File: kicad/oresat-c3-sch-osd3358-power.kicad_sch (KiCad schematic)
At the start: 37 parts, among them Q6 MMBT2907, U1 OSD3358-512M-BSM, U10 SN74LVC1G07DCK, U14 TLVH431

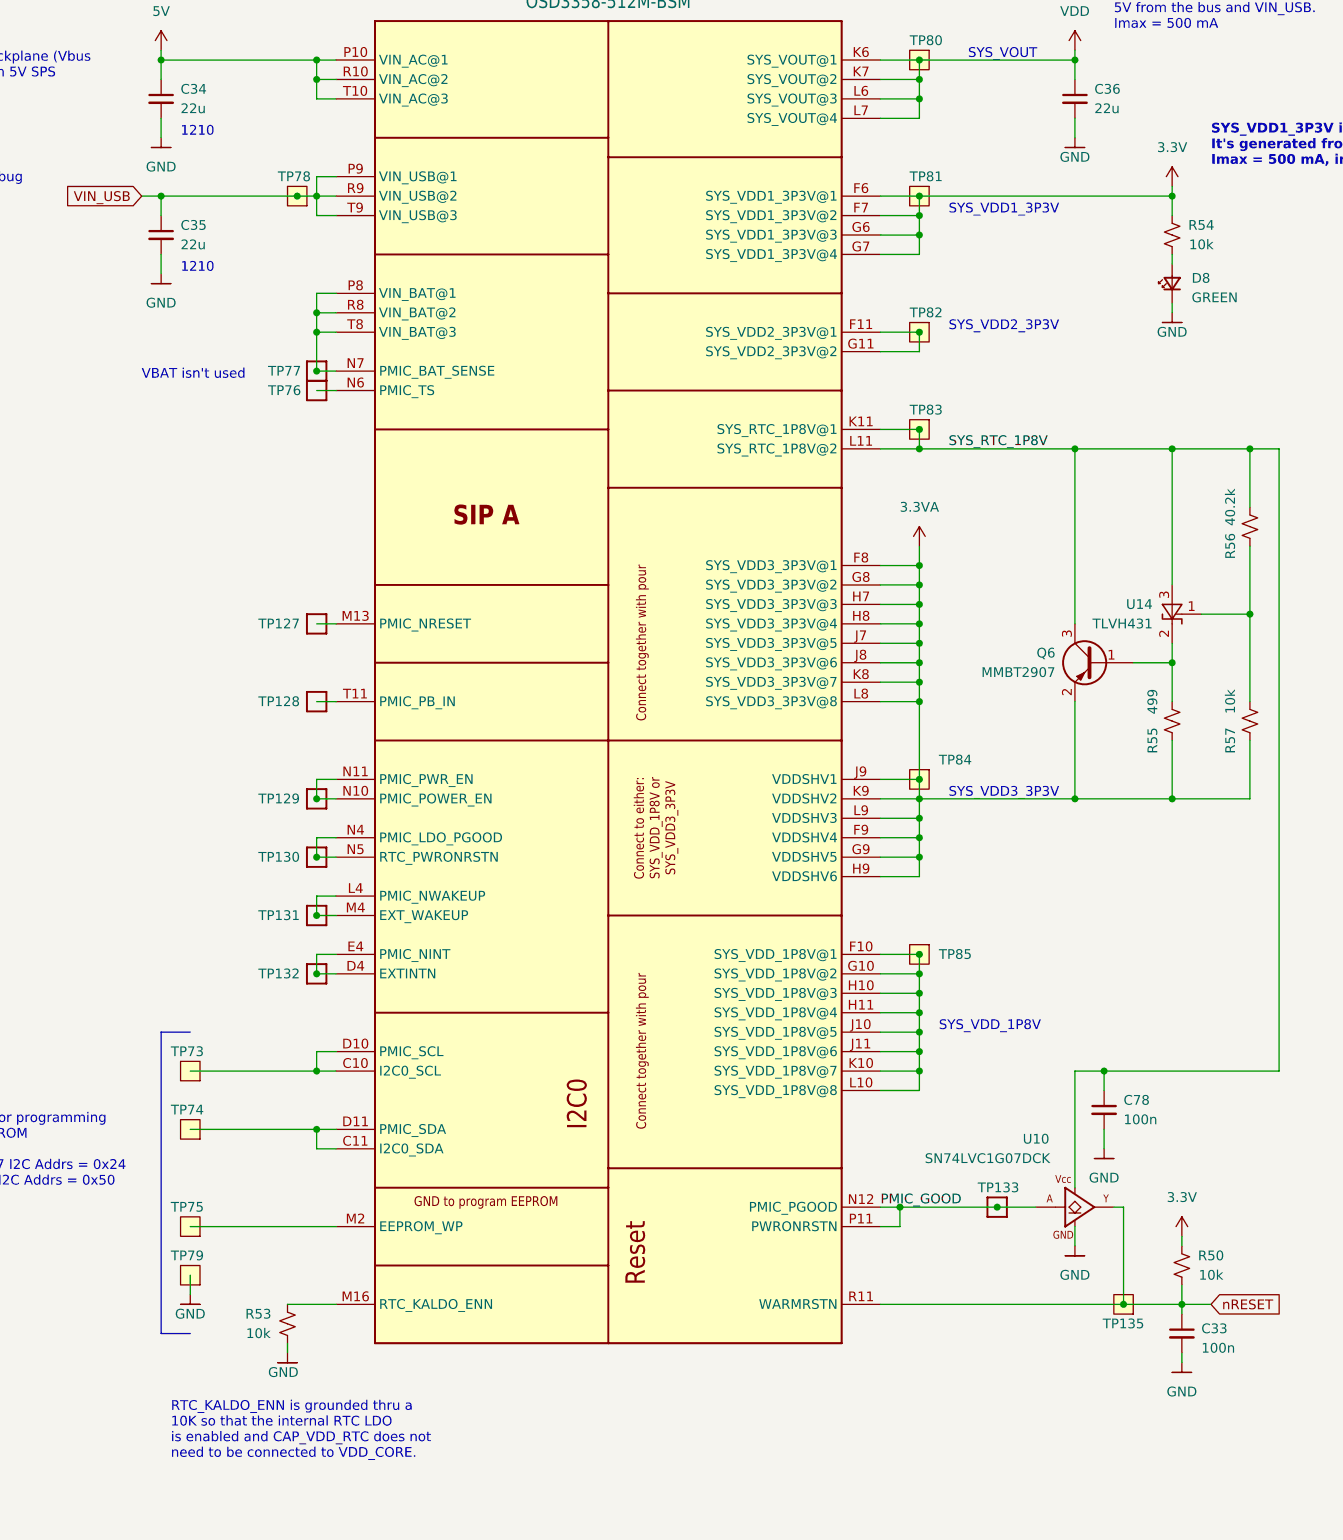
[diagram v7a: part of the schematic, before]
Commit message: Fixed footprints and laid out WDT and OPD circuitry.
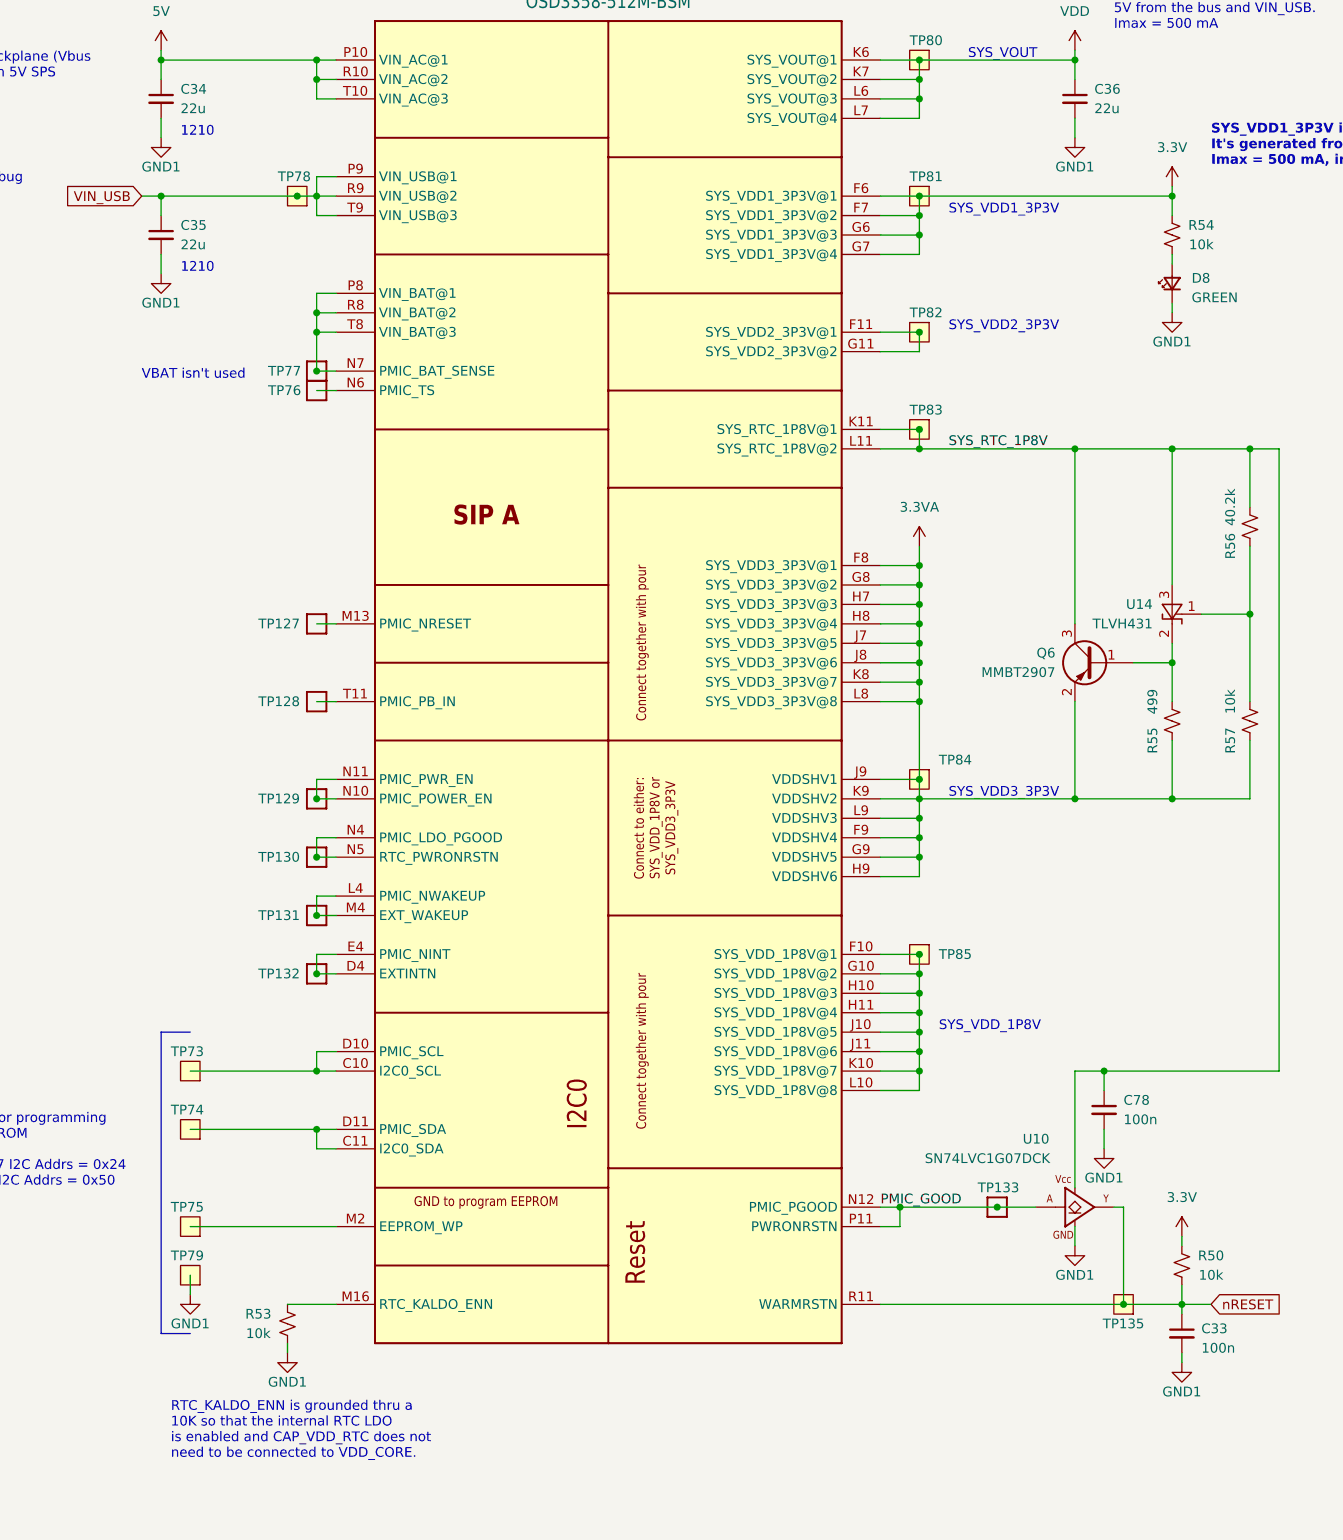
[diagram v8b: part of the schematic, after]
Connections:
- net GND renamed GND1
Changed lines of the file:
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@@
     )
   )
-  (symbol (lib_id "oresat-power:GND") (at 298.45 86.36 0) (unit 1)
-    (in_bom yes) (on_board yes) (dnp no)
-    (property "Reference" "#GND0175" (at 298.45 92.71 0)
-      (effects (font (size 1.27 1.27)) hide)
-    )
-    (property "Value" "GND" (at 298.45 88.9 0)
+  (symbol (lib_id "power:GND1") (at 298.45 86.36 0) (unit 1)
+    (in_bom yes) (on_board yes) (dnp no)
+    (property "Reference" "#PWR0140" (at 298.45 92.71 0)
+      (effects (font (size 1.27 1.27)) hide)
+    )
+    (property "Value" "GND1" (at 298.45 90.17 0)
       (effects (font (size 1.27 1.27)))
     )
@@
       (project "oresat-c3"
         (path "/65d12cdd-c326-4033-9053-c59fa4e0b25e/0c1da208-2d1c-4d05-9cc7-59584e50a6ac"
-          (reference "#GND0175") (unit 1)
+          (reference "#PWR0140") (unit 1)
         )
       )
@@
     )
   )
-  (symbol (lib_id "oresat-power:GND") (at 289.56 195.58 0) (unit 1)
-    (in_bom yes) (on_board yes) (dnp no) (fields_autoplaced)
-    (property "Reference" "#GND0170" (at 289.56 201.93 0)
-      (effects (font (size 1.27 1.27)) hide)
-    )
-    (property "Value" "GND" (at 289.56 199.39 0)
+  (symbol (lib_id "power:GND1") (at 289.56 195.58 0) (unit 1)
+    (in_bom yes) (on_board yes) (dnp no) (fields_autoplaced)
+    (property "Reference" "#PWR0137" (at 289.56 201.93 0)
+      (effects (font (size 1.27 1.27)) hide)
+    )
+    (property "Value" "GND1" (at 289.56 199.39 0)
       (effects (font (size 1.27 1.27)))
     )
@@
       (project "oresat-c3"
         (path "/65d12cdd-c326-4033-9053-c59fa4e0b25e/0c1da208-2d1c-4d05-9cc7-59584e50a6ac"
-          (reference "#GND0170") (unit 1)
+          (reference "#PWR0137") (unit 1)
         )
       )
@@
     )
   )
-  (symbol (lib_id "oresat-power:GND") (at 285.75 63.5 0) (unit 1)
-    (in_bom yes) (on_board yes) (dnp no)
-    (property "Reference" "#GND0174" (at 285.75 69.85 0)
-      (effects (font (size 1.27 1.27)) hide)
-    )
-    (property "Value" "GND" (at 285.75 66.04 0)
+  (symbol (lib_id "power:GND1") (at 285.75 63.5 0) (unit 1)
+    (in_bom yes) (on_board yes) (dnp no)
+    (property "Reference" "#PWR0139" (at 285.75 69.85 0)
+      (effects (font (size 1.27 1.27)) hide)
+    )
+    (property "Value" "GND1" (at 285.75 67.31 0)
       (effects (font (size 1.27 1.27)))
     )
@@
       (project "oresat-c3"
         (path "/65d12cdd-c326-4033-9053-c59fa4e0b25e/0c1da208-2d1c-4d05-9cc7-59584e50a6ac"
-          (reference "#GND0174") (unit 1)
-        )
-      )
-    )
-  )
-  (symbol (lib_id "oresat-power:GND") (at 182.88 222.25 0) (unit 1)
-    (in_bom yes) (on_board yes) (dnp no)
-    (property "Reference" "#GND0171" (at 182.88 228.6 0)
-      (effects (font (size 1.27 1.27)) hide)
-    )
-    (property "Value" "GND" (at 180.34 224.79 0)
-      (effects (font (size 1.27 1.27)) (justify left))
+          (reference "#PWR0139") (unit 1)
+        )
+      )
+    )
+  )
+  (symbol (lib_id "power:GND1") (at 182.88 222.25 0) (unit 1)
+    (in_bom yes) (on_board yes) (dnp no)
+    (property "Reference" "#PWR0143" (at 182.88 228.6 0)
+      (effects (font (size 1.27 1.27)) hide)
+    )
+    (property "Value" "GND1" (at 182.88 226.06 0)
+      (effects (font (size 1.27 1.27)))
     )
     (property "Footprint" "" (at 182.88 222.25 0)
@@
       (project "oresat-c3"
         (path "/65d12cdd-c326-4033-9053-c59fa4e0b25e/0c1da208-2d1c-4d05-9cc7-59584e50a6ac"
-          (reference "#GND0171") (unit 1)
-        )
-      )
-    )
-  )
-  (symbol (lib_id "oresat-power:GND") (at 166.37 81.28 0) (unit 1)
-    (in_bom yes) (on_board yes) (dnp no) (fields_autoplaced)
-    (property "Reference" "#GND0165" (at 166.37 87.63 0)
-      (effects (font (size 1.27 1.27)) hide)
-    )
-    (property "Value" "GND" (at 166.37 85.09 0)
+          (reference "#PWR0143") (unit 1)
+        )
+      )
+    )
+  )
+  (symbol (lib_id "power:GND1") (at 166.37 81.28 0) (unit 1)
+    (in_bom yes) (on_board yes) (dnp no) (fields_autoplaced)
+    (property "Reference" "#PWR0142" (at 166.37 87.63 0)
+      (effects (font (size 1.27 1.27)) hide)
+    )
+    (property "Value" "GND1" (at 166.37 85.09 0)
       (effects (font (size 1.27 1.27)))
     )
@@
       (project "oresat-c3"
         (path "/65d12cdd-c326-4033-9053-c59fa4e0b25e/0c1da208-2d1c-4d05-9cc7-59584e50a6ac"
-          (reference "#GND0165") (unit 1)
+          (reference "#PWR0142") (unit 1)
         )
       )
@@
     )
   )
-  (symbol (lib_id "oresat-power:GND") (at 299.72 223.52 0) (unit 1)
-    (in_bom yes) (on_board yes) (dnp no) (fields_autoplaced)
-    (property "Reference" "#GND038" (at 299.72 229.87 0)
-      (effects (font (size 1.27 1.27)) hide)
-    )
-    (property "Value" "GND" (at 299.72 227.33 0)
+  (symbol (lib_id "power:GND1") (at 299.72 223.52 0) (unit 1)
+    (in_bom yes) (on_board yes) (dnp no) (fields_autoplaced)
+    (property "Reference" "#PWR0136" (at 299.72 229.87 0)
+      (effects (font (size 1.27 1.27)) hide)
+    )
+    (property "Value" "GND1" (at 299.72 227.33 0)
       (effects (font (size 1.27 1.27)))
     )
@@
       (project "oresat-c3"
         (path "/65d12cdd-c326-4033-9053-c59fa4e0b25e/0c1da208-2d1c-4d05-9cc7-59584e50a6ac"
-          (reference "#GND038") (unit 1)
+          (reference "#PWR0136") (unit 1)
         )
       )
@@
     )
   )
-  (symbol (lib_id "oresat-power:GND") (at 285.75 208.28 0) (unit 1)
-    (in_bom yes) (on_board yes) (dnp no) (fields_autoplaced)
-    (property "Reference" "#GND0169" (at 285.75 214.63 0)
-      (effects (font (size 1.27 1.27)) hide)
-    )
-    (property "Value" "GND" (at 285.75 212.09 0)
+  (symbol (lib_id "power:GND1") (at 285.75 208.28 0) (unit 1)
+    (in_bom yes) (on_board yes) (dnp no) (fields_autoplaced)
+    (property "Reference" "#PWR0138" (at 285.75 214.63 0)
+      (effects (font (size 1.27 1.27)) hide)
+    )
+    (property "Value" "GND1" (at 285.75 212.09 0)
       (effects (font (size 1.27 1.27)))
     )
@@
       (project "oresat-c3"
         (path "/65d12cdd-c326-4033-9053-c59fa4e0b25e/0c1da208-2d1c-4d05-9cc7-59584e50a6ac"
-          (reference "#GND0169") (unit 1)
+          (reference "#PWR0138") (unit 1)
         )
       )
@@
     )
   )
-  (symbol (lib_id "oresat-power:GND") (at 166.37 63.5 0) (unit 1)
-    (in_bom yes) (on_board yes) (dnp no) (fields_autoplaced)
-    (property "Reference" "#GND0166" (at 166.37 69.85 0)
-      (effects (font (size 1.27 1.27)) hide)
-    )
-    (property "Value" "GND" (at 166.37 67.31 0)
+  (symbol (lib_id "power:GND1") (at 166.37 63.5 0) (unit 1)
+    (in_bom yes) (on_board yes) (dnp no) (fields_autoplaced)
+    (property "Reference" "#PWR0141" (at 166.37 69.85 0)
+      (effects (font (size 1.27 1.27)) hide)
+    )
+    (property "Value" "GND1" (at 166.37 67.31 0)
       (effects (font (size 1.27 1.27)))
     )
@@
       (project "oresat-c3"
         (path "/65d12cdd-c326-4033-9053-c59fa4e0b25e/0c1da208-2d1c-4d05-9cc7-59584e50a6ac"
-          (reference "#GND0166") (unit 1)
+          (reference "#PWR0141") (unit 1)
         )
       )
@@
     )
   )
-  (symbol (lib_id "oresat-power:GND") (at 170.18 214.63 0) (unit 1)
-    (in_bom yes) (on_board yes) (dnp no)
-    (property "Reference" "#GND037" (at 170.18 220.98 0)
-      (effects (font (size 1.27 1.27)) hide)
-    )
-    (property "Value" "GND" (at 170.18 217.17 0)
+  (symbol (lib_id "power:GND1") (at 170.18 214.63 0) (unit 1)
+    (in_bom yes) (on_board yes) (dnp no)
+    (property "Reference" "#PWR0144" (at 170.18 220.98 0)
+      (effects (font (size 1.27 1.27)) hide)
+    )
+    (property "Value" "GND1" (at 170.18 218.44 0)
       (effects (font (size 1.27 1.27)))
     )
@@
       (project "oresat-c3"
         (path "/65d12cdd-c326-4033-9053-c59fa4e0b25e/0c1da208-2d1c-4d05-9cc7-59584e50a6ac"
-          (reference "#GND037") (unit 1)
-        )
-      )
+          (reference "#PWR0144") (unit 1)
+        )
+      )
